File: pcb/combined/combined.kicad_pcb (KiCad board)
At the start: 2 copper layers, 124.8 x 87.6 mm, 80 parts, among them J1 5V SCREEN, J10 PRESSURE, J11 XIAO D0-D6, J12 XIAO D7-5V, J2 MAINS_IN, J3 VALVE, J5 CAN BUS, J6 FLOW HALL, J7 24V IN, J8 BOILER SSR, J9 PUMP, Q1 SS8050, Q2 BT136S, Q5 AO3401A, Q6 2N7002, U1 MOC3043M, U10 LMR33630ADDAR, U4 TJA1051T/3, U5 TMP102AIDRLR, U6 ADS1115IDGST, U8 EL817C, U9 EL817C

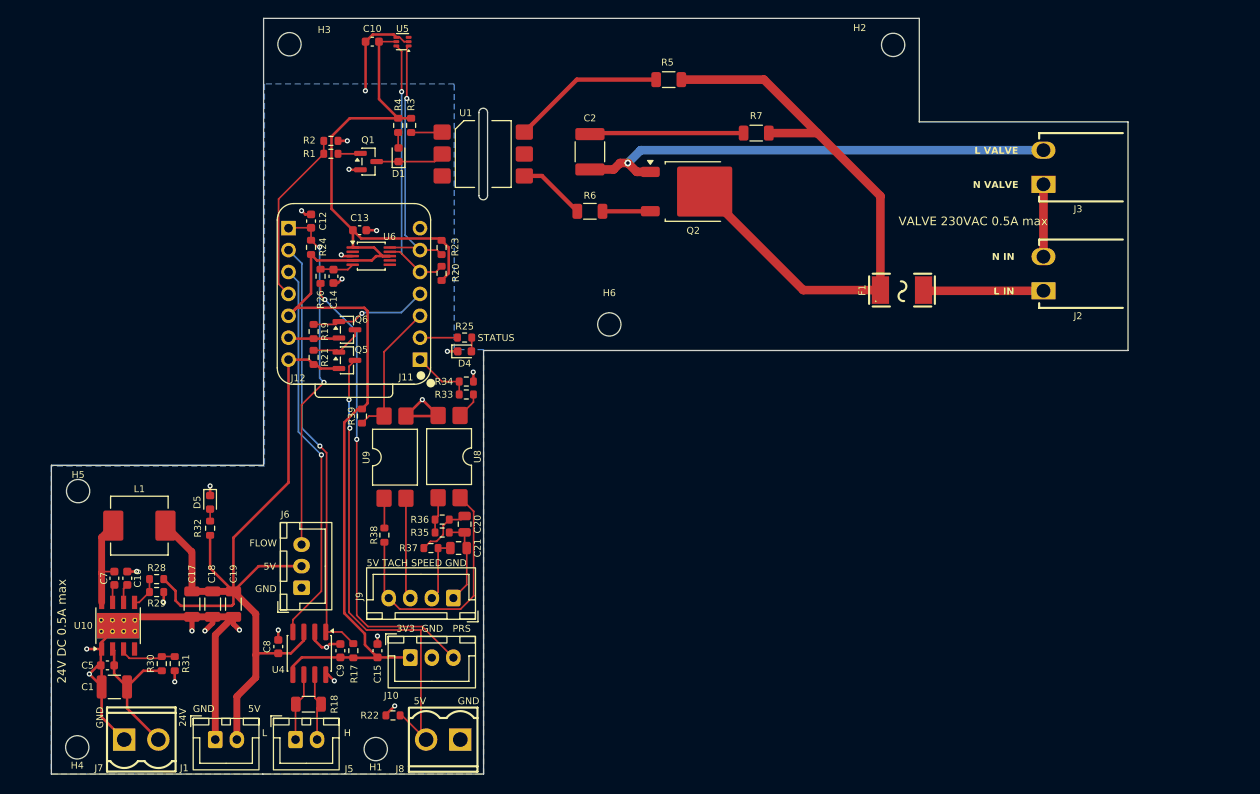
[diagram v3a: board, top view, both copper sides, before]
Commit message: Move combined to basic passives, M2 holes and an HT3.96 flow connector
- Mounting holes H1 to H6 become M2 (2.2 mm NPTH) and move on the board;
  the AC wing narrows to 35 mm.
- Nine extended passives become JLCPCB basic parts: R3 150, R5/R6
  300 + 300, R7 100 (1206 kept: an 0805 breaks the 1.5 mm L-side
  clearance), FB divider 120k/30k (5.00 V), EN divider 330k/24k
  (18.2 V / 16.7 V), C1 10 uF 1206, C5 220 nF 0805, setpoint filter
  1.5k / 2.2 uF. Only C2 (10 nF 1 kV) stays extended.
- J6 (flow) becomes a Kefa HT396V-3.96-3P: the Digmesa 0.5 mm2 wires
  screw into the plug without the JST-SM to XH adapter. Footprint and
  3D model from LCSC, checked against the Kefa drawing.
- The MPB003 manufacturer datasheet replaces gearpump.pdf; it confirms
  the 7-wire pinout used on J9.

Co-Authored-By: Claude Opus 5.5 <noreply@anthropic.com>
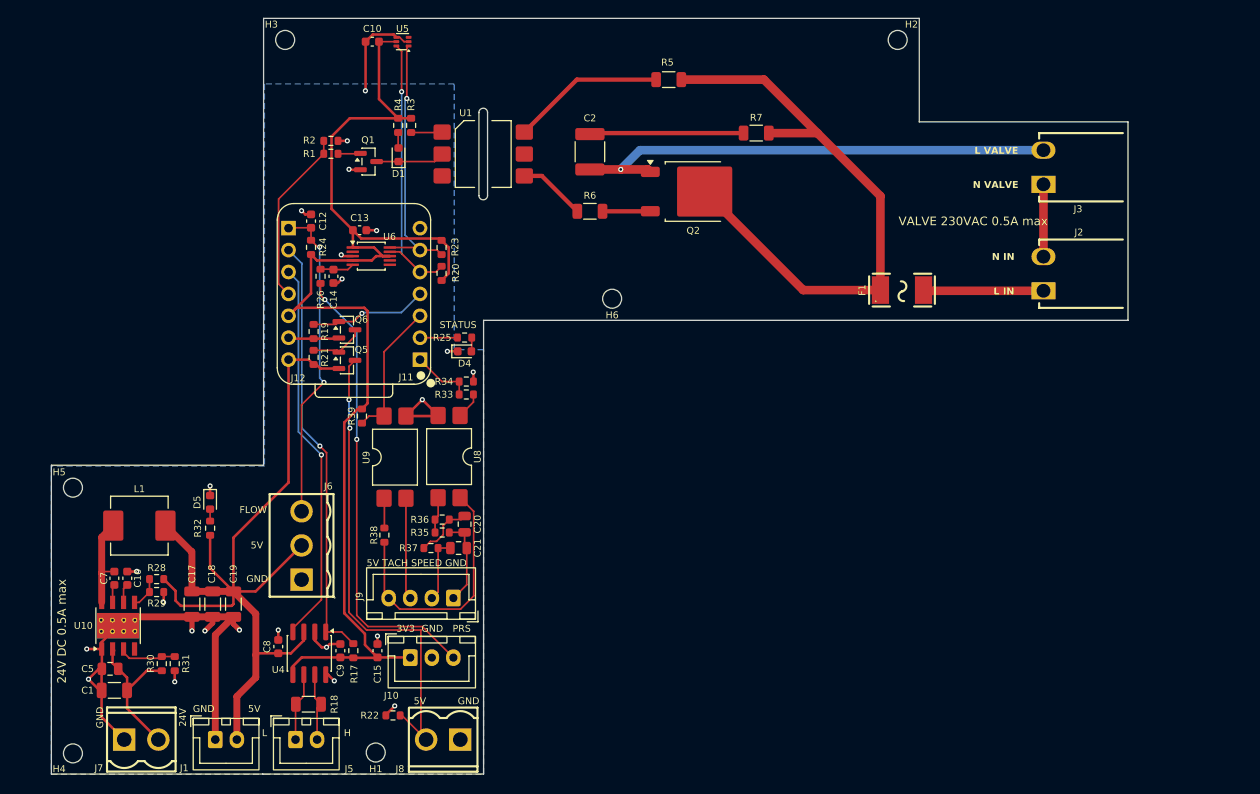
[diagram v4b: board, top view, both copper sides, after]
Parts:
- C1: footprint Capacitor_SMD:C_1210_3225Metric -> Capacitor_SMD:C_1206_3216Metric
- C20, C21: value 1.5uF -> 2.2uF
- C5: footprint Capacitor_SMD:C_0603_1608Metric -> Capacitor_SMD:C_0805_2012Metric
- H1, H2, H3, H4, H5, H6: value M2.5 -> M2; footprint MountingHole:MountingHole_2.7mm_M2.5 -> MountingHole:MountingHole_2.2mm_M2
- J6: footprint Connector_JST:JST_XH_B3B-XH-A_1x03_P2.50mm_Vertical -> Combined_Local:CONN-TH_P3.96_HT396V-3.96-3P
- R28: value 100k -> 120k
- R29: value 24.9k -> 30k
- R3: value 180 -> 150
- R30: value 100k -> 330k
- R31: value 7.15k -> 24k
- R36, R37: value 2.2k -> 1.5k
- R5: value 360 -> 300
- R6: value 330 -> 300
- R7: value 39 -> 100
- moved J6 4.90 mm to (84.9, 108.1)
- moved H6 2.99 mm to (120.9, 79.5)
- moved H4 0.86 mm to (58.4, 132.2)
- moved H2 0.78 mm to (154.0, 49.5)
- moved H5 0.72 mm to (58.4, 101.4)
- moved H3 0.71 mm to (83.0, 49.5)
- moved C5 0.50 mm to (62.7, 122.4)
- moved C1 0.40 mm to (63.2, 124.9)
- moved H1 0.40 mm to (93.5, 132.1)
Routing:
- net FLOW_PULSE: track 41.2 -> 37.3 mm
- net +5V: track 104.2 -> 105.1 mm
- net GND: track 105.2 -> 105.8 mm
- net /L_VALVE: track 56.5 -> 57.0 mm
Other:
- outline, holes or cut-outs redrawn
